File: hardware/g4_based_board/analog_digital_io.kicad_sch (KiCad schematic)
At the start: 0 parts

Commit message: auto updated files
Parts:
- added D8: RCLAMP0502B, Package_TO_SOT_SMD:SOT-416, symbol Power_Protection:RCLAMP0502B
- added J13: Conn_01x02_Pin, symbol Connector:Conn_01x02_Pin
- added Q5, Q6: DMN6075S, Package_TO_SOT_SMD:SOT-23, symbol Transistor_FET:DMN6075S
- added SW3, SW4: SW_SPDT, symbol Switch:SW_SPDT
- added SW5, SW6: SW_DIP_x01, symbol Switch:SW_DIP_x01
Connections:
- new net: D8.2 (K2), J13.1 (Pin_1), Q6.2 (S)
- new net: D8.1 (K1), J13.2 (Pin_2), Q5.2 (S)
- new net: Q6.1 (G), SW6.2
- new net: Q6.3 (D), SW4.2 (B)
- new net: Q5.1 (G), SW5.2
- new net: Q5.3 (D), SW3.2 (B)
- new net +3.3V: SW3.1 (A), SW4.1 (A)
- new net GND: D8.3 (A)
- new net VBAT: SW3.3 (C), SW4.3 (C)
- new net sig_diff_1: SW5.1
- new net sig_diff_2: SW6.1

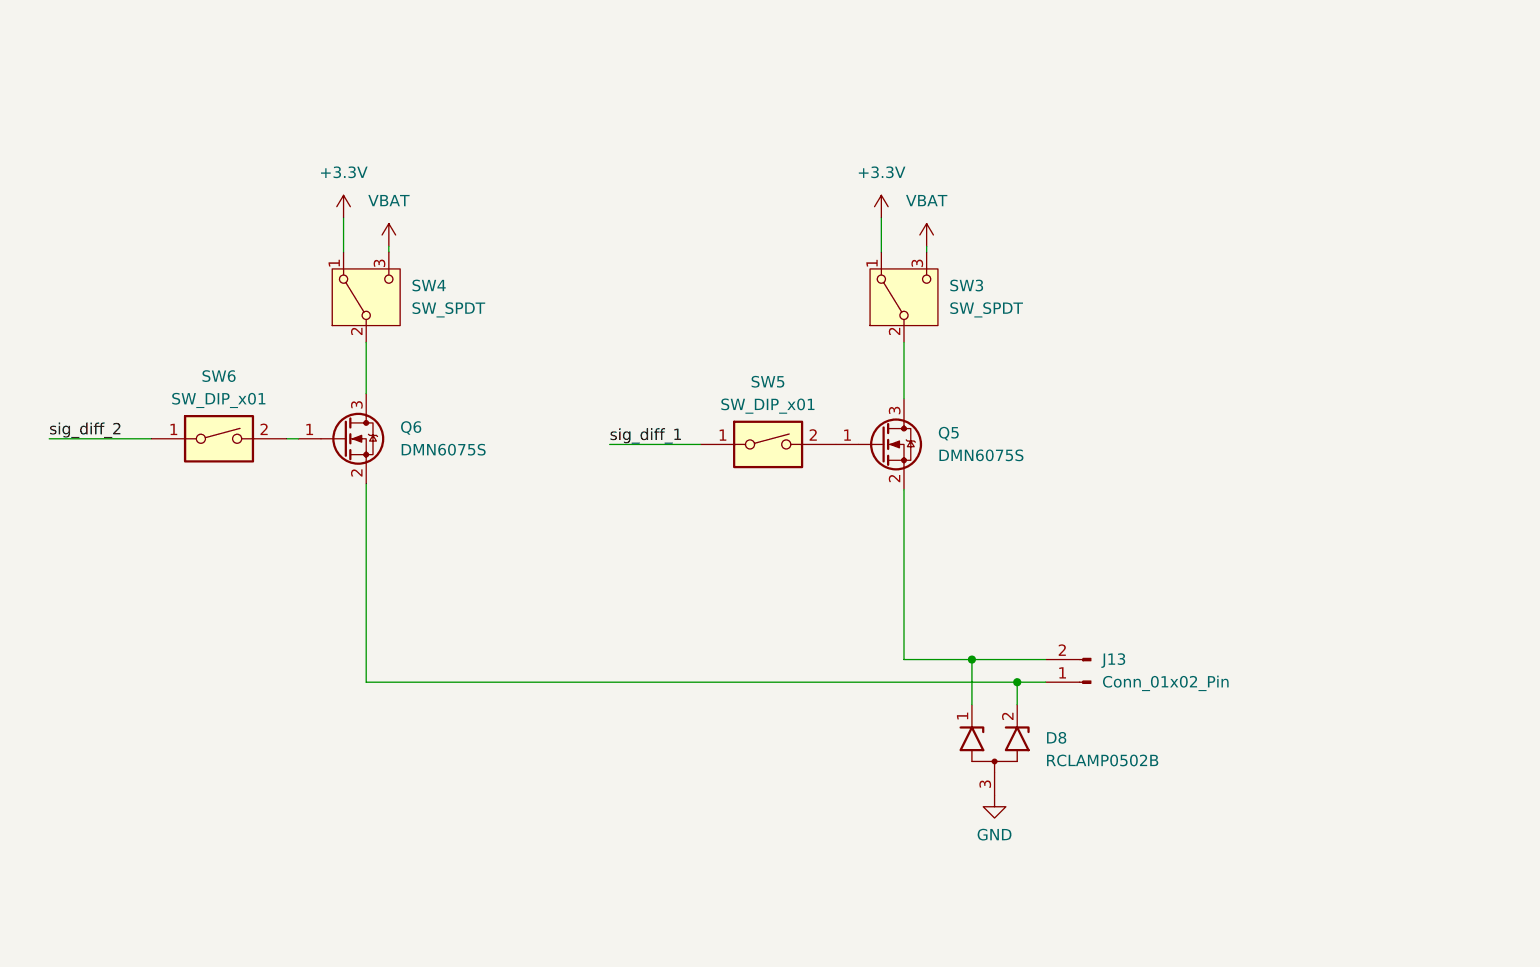
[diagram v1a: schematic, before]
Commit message: first desgin of a multi use interface to allow signal and power out on the same lines
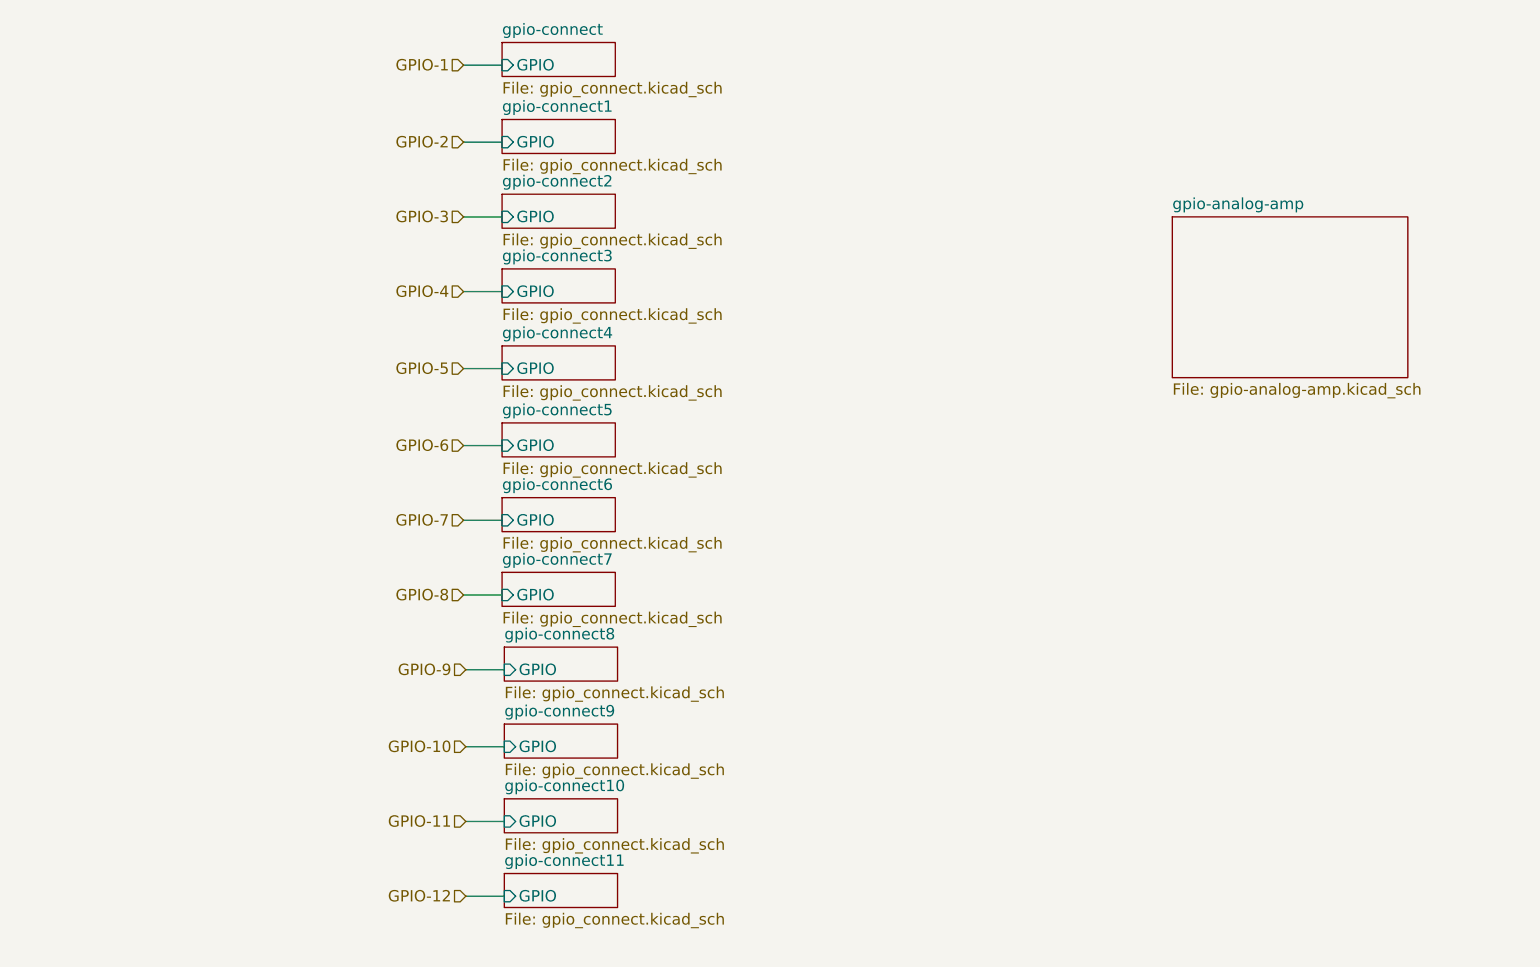
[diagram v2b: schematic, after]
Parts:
- removed D8: RCLAMP0502B, Package_TO_SOT_SMD:SOT-416, symbol Power_Protection:RCLAMP0502B
- removed J13: Conn_01x02_Pin, symbol Connector:Conn_01x02_Pin
- removed Q5, Q6: DMN6075S, Package_TO_SOT_SMD:SOT-23, symbol Transistor_FET:DMN6075S
- removed SW3, SW4: SW_SPDT, symbol Switch:SW_SPDT
- removed SW5, SW6: SW_DIP_x01, symbol Switch:SW_DIP_x01
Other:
- added sheet gpio-analog-amp (gpio-analog-amp.kicad_sch)
- added sheet gpio-connect (gpio_connect.kicad_sch)
- added sheet gpio-connect1 (gpio_connect.kicad_sch)
- added sheet gpio-connect10 (gpio_connect.kicad_sch)
- added sheet gpio-connect11 (gpio_connect.kicad_sch)
- added sheet gpio-connect2 (gpio_connect.kicad_sch)
- added sheet gpio-connect3 (gpio_connect.kicad_sch)
- added sheet gpio-connect4 (gpio_connect.kicad_sch)
- added sheet gpio-connect5 (gpio_connect.kicad_sch)
- added sheet gpio-connect6 (gpio_connect.kicad_sch)
- added sheet gpio-connect7 (gpio_connect.kicad_sch)
- added sheet gpio-connect8 (gpio_connect.kicad_sch)
- added sheet gpio-connect9 (gpio_connect.kicad_sch)

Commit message: now uses hierarchical sheets
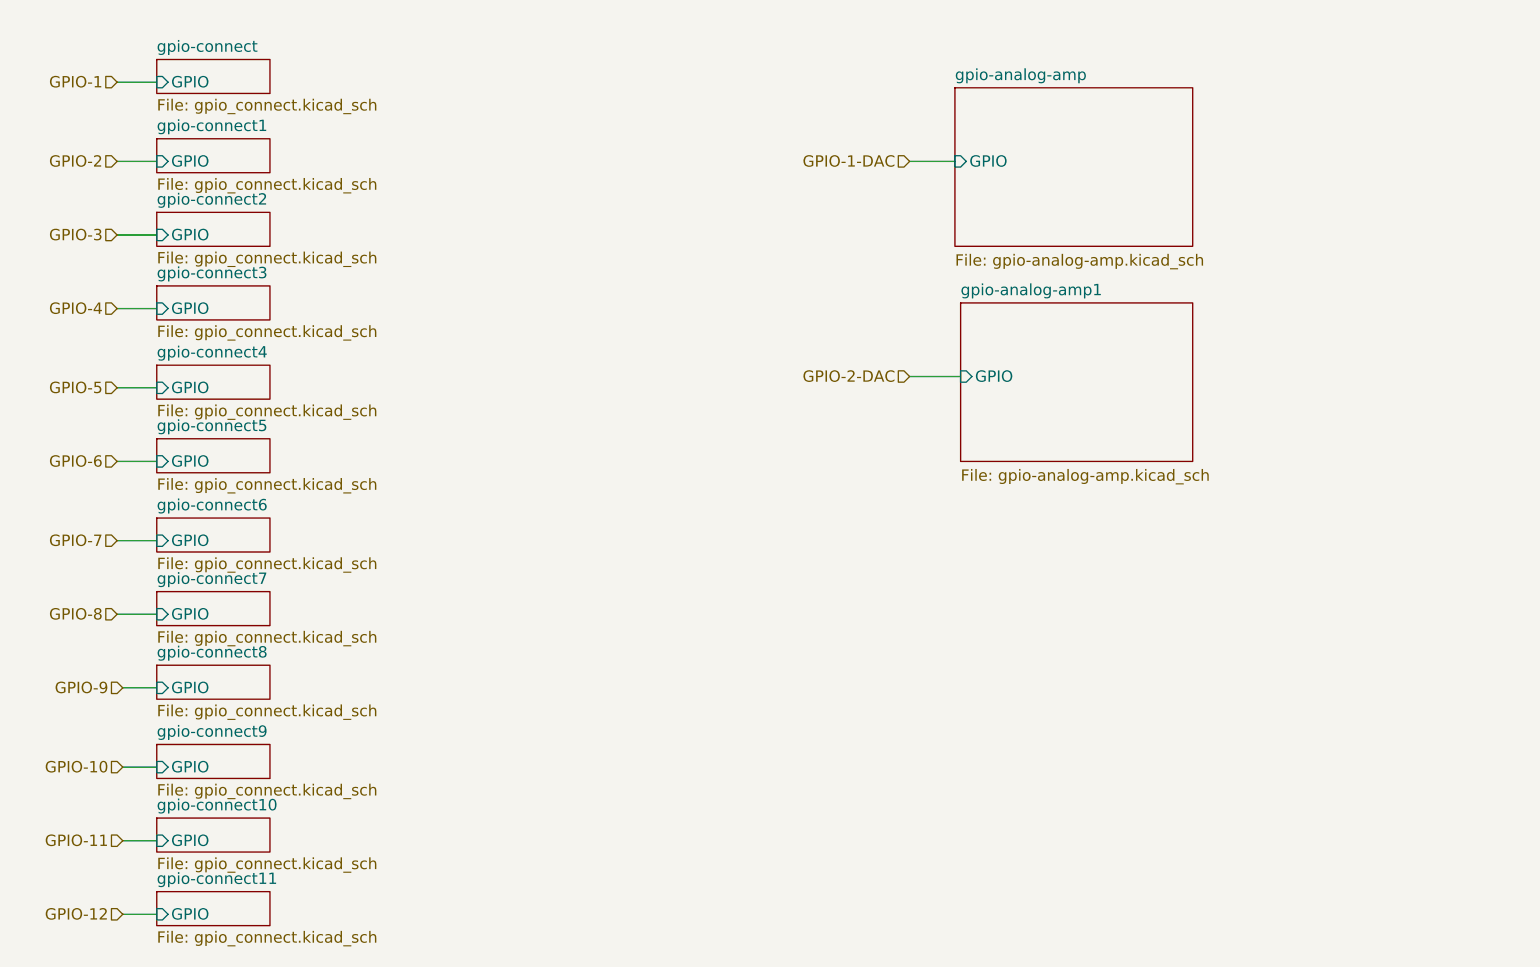
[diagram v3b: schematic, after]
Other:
- added sheet gpio-analog-amp1 (gpio-analog-amp.kicad_sch)
- sheet gpio-analog-amp ports: added GPIO; removed none

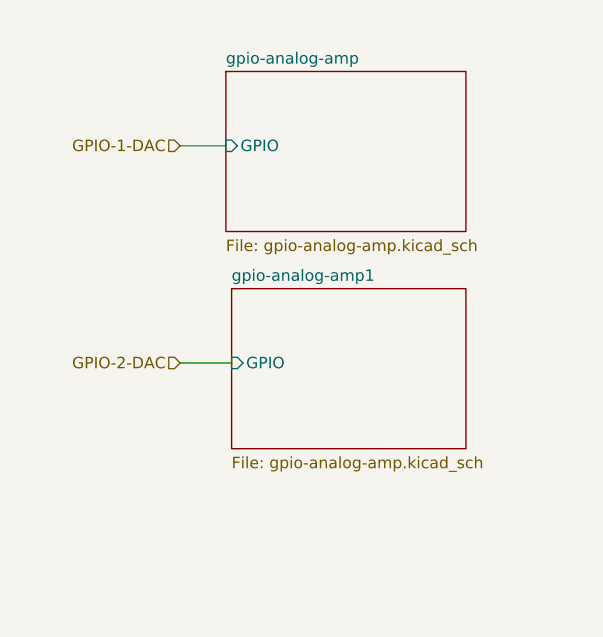
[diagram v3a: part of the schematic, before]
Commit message: changed the dac outputs to normal gpio as there was not enough room
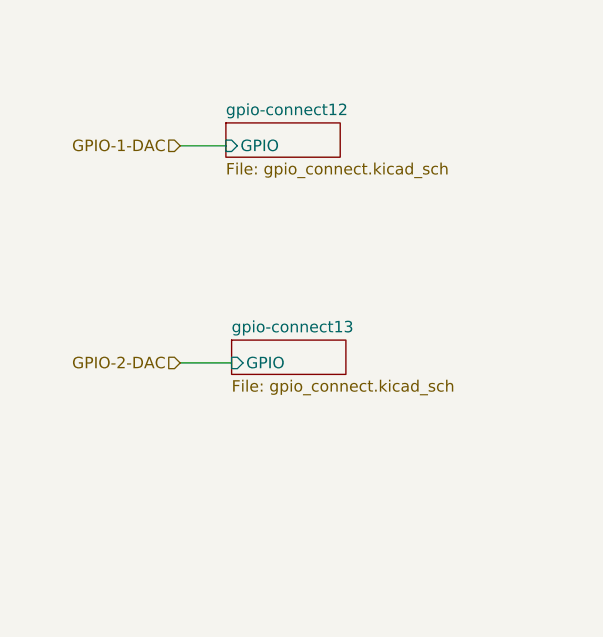
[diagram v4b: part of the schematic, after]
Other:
- removed sheet gpio-analog-amp
- removed sheet gpio-analog-amp1
- added sheet gpio-connect12 (gpio_connect.kicad_sch)
- added sheet gpio-connect13 (gpio_connect.kicad_sch)
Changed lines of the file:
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@@
 	)
 	(sheet
-		(at 160.02 49.53)
-		(size 26.67 17.78)
-		(fields_autoplaced yes)
-		(stroke
-			(width 0.1524)
-			(type solid)
-		)
-		(fill
-			(color 0 0 0 0.0000)
-		)
-		(property "Sheetname" "gpio-analog-amp"
-			(at 160.02 48.8184 0)
-			(effects
-				(font
-					(size 1.27 1.27)
-				)
-				(justify left bottom)
-			)
-		)
-		(property "Sheetfile" "gpio-analog-amp.kicad_sch"
-			(at 160.02 68.1486 0)
+		(at 160.02 55.245)
+		(size 12.7 3.81)
+		(fields_autoplaced yes)
+		(stroke
+			(width 0.1524)
+			(type solid)
+		)
+		(fill
+			(color 0 0 0 0.0000)
+		)
+		(property "Sheetname" "gpio-connect12"
+			(at 160.02 54.5334 0)
+			(effects
+				(font
+					(size 1.27 1.27)
+				)
+				(justify left bottom)
+			)
+		)
+		(property "Sheetfile" "gpio_connect.kicad_sch"
+			(at 160.02 59.6396 0)
 			(effects
 				(font
@@
 			(project "data_logger"
 				(path "/9bc93932-ff5f-4f35-96cf-dfa5f042acb6/9b7d6bd0-4bb6-4940-8a64-141003fad1a5"
-					(page "23")
+					(page "8")
 				)
 			)
@@
 	)
 	(sheet
-		(at 160.655 73.66)
-		(size 26.035 17.78)
-		(fields_autoplaced yes)
-		(stroke
-			(width 0.1524)
-			(type solid)
-		)
-		(fill
-			(color 0 0 0 0.0000)
-		)
-		(property "Sheetname" "gpio-analog-amp1"
-			(at 160.655 72.9484 0)
-			(effects
-				(font
-					(size 1.27 1.27)
-				)
-				(justify left bottom)
-			)
-		)
-		(property "Sheetfile" "gpio-analog-amp.kicad_sch"
-			(at 160.655 92.2786 0)
+		(at 160.655 79.375)
+		(size 12.7 3.81)
+		(fields_autoplaced yes)
+		(stroke
+			(width 0.1524)
+			(type solid)
+		)
+		(fill
+			(color 0 0 0 0.0000)
+		)
+		(property "Sheetname" "gpio-connect13"
+			(at 160.655 78.6634 0)
+			(effects
+				(font
+					(size 1.27 1.27)
+				)
+				(justify left bottom)
+			)
+		)
+		(property "Sheetfile" "gpio_connect.kicad_sch"
+			(at 160.655 83.7696 0)
 			(effects
 				(font
@@
 			(project "data_logger"
 				(path "/9bc93932-ff5f-4f35-96cf-dfa5f042acb6/9b7d6bd0-4bb6-4940-8a64-141003fad1a5"
-					(page "8")
-				)
-			)
+					(page "23")
+				)
+			)
